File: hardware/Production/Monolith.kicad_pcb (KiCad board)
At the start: 6 copper layers, 43.2 x 74.4 mm, 289 parts, among them J102 Cell 1 NTC wires, J105 Cell 2 NTC wires, J106 Cell 3 NTC wires, J107 Cell 4 NTC wires, J108 PACK- power slot, J109 CELL1 slot, J110 CELL2 slot, J111 CELL3 slot, J112 PACK+ power slot, J113 LOAD PACK_P, J114 LOAD GND, J115 1N Kelvin slot, J116 4P Kelvin slot, J301 TC2030-NL, J302 TC2030-NL GAUGE, J401 TYPE-C 16PCB1.6 IP68, J501 TYPE-C 16PCB1.6 IP68, Q101 AGM404AP1, Q102 AGM404AP1, Q103 AO3400A, Q104 AO3400A, Q401 SiZ240DT, Q402 SiZ240DT, Q501 SiZ240DT, Q502 SiZ240DT, U101 BQ40Z50RSMR-R2, U102 BQ294700DSGR, U204 TPS62177DQCR, U301 CC2340R5MODA, U401 TPS25751DREFR, U402 M24512-DFMC6TG, U403 BQ25756RRVR, U404 TPS62933DRLR, U405 TPD6S300RUKR, U501 TPS25751DREFR, U502 M24512-DFMC6TG, U503 BQ25756RRVR, U504 TPS62933DRLR, U505 TPD6S300RUKR

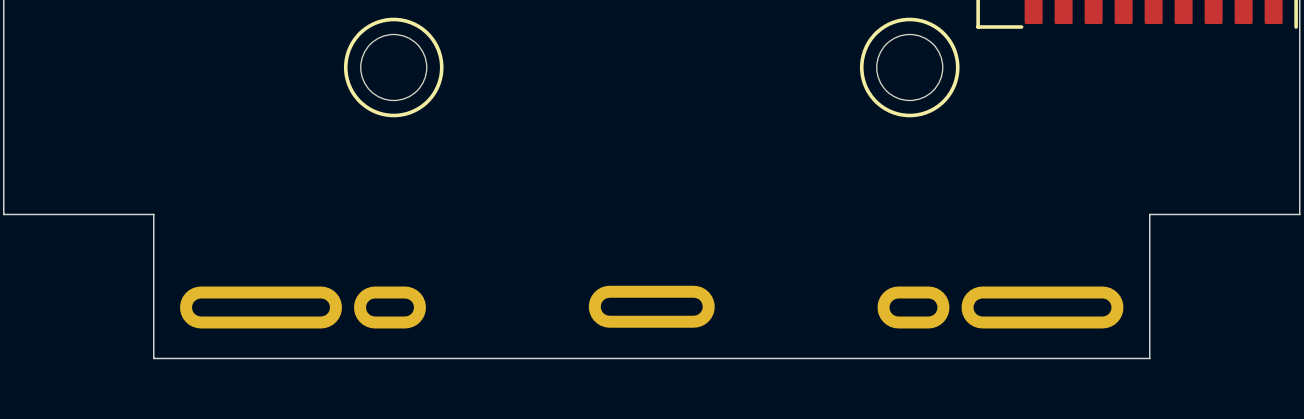
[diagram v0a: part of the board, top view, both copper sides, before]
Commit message: Production board: PACK wire holes for the option C wire tails
J108 / J112 go from the 4.6 mm PACK power slots to Ø1.5 mm plated holes
(0.4 mm ring) for the 18 AWG thin-wall PTFE power wires, at sb_pack_holes():
KiCad (86.975, 135.7255) and (113.025, 135.7255), F.Cu, locked. The Kelvin
wires stay in the J115 / J116 slots.

- make_production.py: WIRE_FP footprint generated from SB_PWIRE_*, used for
  J108 / J112; SLOT_REFS keeps the five slots, WIRE_REFS the two holes.
- make_board.py: --mech also places the wire holes; keepout_list() follows
  the merged model (three tail runs, four KO_B_wire_* from sb_wire_runs()).
- Board: J108 / J112 swapped and placed as Update PCB + --mech would; the four
  PACK / Kelvin finger tail keep-outs replaced by KO_B_wire_*. Other
  keep-outs untouched (KO_F_above_antenna stays removed).
- Schematic Footprint / Value fields and sheet notes; Slot_Tab_4.6x0.6mm
  dropped from the library; README, spec and assembly docs.

KiCad is not available in this environment, so DRC has not been run; a
script check covers the outline, edge rule, ring and courtyards.

Co-Authored-By: Claude Opus 5.5 (1M context) <noreply@anthropic.com>
Claude-Session: https://claude.ai/code/session_01VT5ZsG8mLjRjzAJFn7LJRo
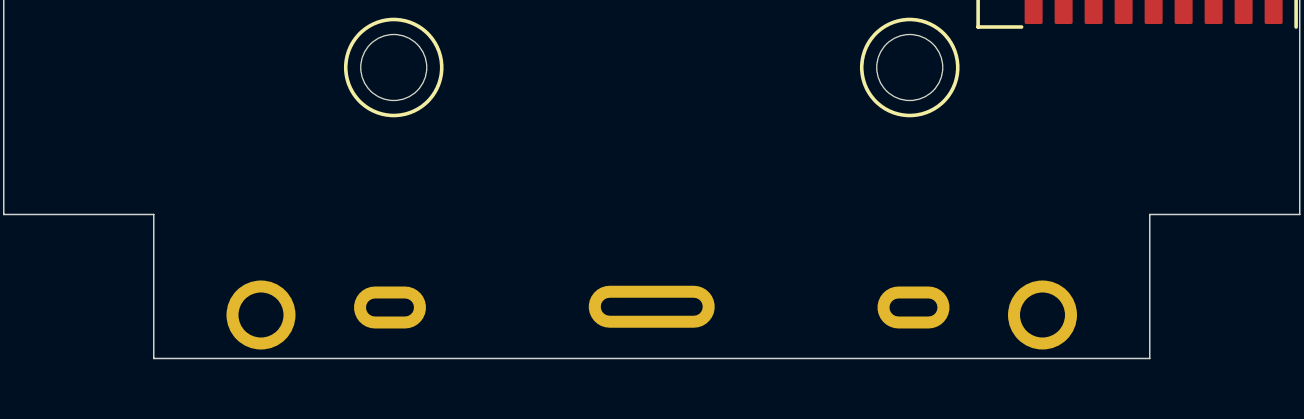
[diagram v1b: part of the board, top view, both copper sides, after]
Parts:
- J108: value PACK- power slot -> PACK- power wire; footprint MonolithDev:Slot_Tab_4.6x0.6mm -> MonolithDev:SolderWire-18AWG_PTFE_1x01_D1.5mm_OD2.3mm
- J112: value PACK+ power slot -> PACK+ power wire; footprint MonolithDev:Slot_Tab_4.6x0.6mm -> MonolithDev:SolderWire-18AWG_PTFE_1x01_D1.5mm_OD2.3mm
- moved J108 0.25 mm to (87.0, 135.7)
- moved J112 0.25 mm to (113.0, 135.7)
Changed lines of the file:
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@@
 		)
 	)
-	(footprint "MonolithDev:Slot_Tab_4.6x0.6mm"
+	(footprint "MonolithDev:SolderWire-18AWG_PTFE_1x01_D1.5mm_OD2.3mm"
 		(locked yes)
 		(layer "F.Cu")
-		(at 113.025 135.4755)
-		(descr "Plated slot 4.6 x 0.6 mm, 0.4 mm ring, for a nickel tail soldered on F.Cu (mechanical/monolith_shell.py sb_slots)")
-		(tags "slot nickel tab battery")
+		(at 113.025 135.7255)
+		(descr "Plated hole 1.5 mm, 0.4 mm ring, for an 18 AWG thin-wall PTFE PACK wire (M22759/11-18, 1.45 mm OD at most) soldered on F.Cu (mechanical/monolith_shell.py sb_pack_holes)")
+		(tags "connector wire 18AWG PTFE battery")
 		(property "Reference" "J112"
-			(at 0 -1.4 0)
+			(at 0 -2 0)
 			(layer "F.SilkS")
 			(hide yes)
@@
 			)
 		)
-		(property "Value" "PACK+ power slot"
-			(at 0 1.4 0)
+		(property "Value" "PACK+ power wire"
+			(at 0 2 0)
 			(layer "F.Fab")
 			(effects
@@
 		(duplicate_pad_numbers_are_jumpers no)
 		(fp_rect
-			(start -2.8 -0.8)
-			(end 2.8 0.8)
+			(start -1.4 -1.4)
+			(end 1.4 1.4)
 			(stroke
 				(width 0.05)
@@
 			(layer "F.CrtYd")
 		)
-		(fp_rect
-			(start -2.3 -0.3)
-			(end 2.3 0.3)
+		(fp_circle
+			(center 0 0)
+			(end 0.725 0)
 			(stroke
 				(width 0.1)
@@
 			)
 		)
-		(pad "1" thru_hole oval
+		(pad "1" thru_hole circle
 			(at 0 0)
-			(size 5.4 1.4)
-			(drill oval 4.6 0.6)
+			(size 2.3 2.3)
+			(drill 1.5)
 			(layers "*.Cu" "*.Mask")
 			(remove_unused_layers no)
@@
 		)
 	)
-	(footprint "MonolithDev:Slot_Tab_4.6x0.6mm"
+	(footprint "MonolithDev:SolderWire-18AWG_PTFE_1x01_D1.5mm_OD2.3mm"
 		(locked yes)
 		(layer "F.Cu")
-		(at 86.975 135.4755)
-		(descr "Plated slot 4.6 x 0.6 mm, 0.4 mm ring, for a nickel tail soldered on F.Cu (mechanical/monolith_shell.py sb_slots)")
-		(tags "slot nickel tab battery")
+		(at 86.975 135.7255)
+		(descr "Plated hole 1.5 mm, 0.4 mm ring, for an 18 AWG thin-wall PTFE PACK wire (M22759/11-18, 1.45 mm OD at most) soldered on F.Cu (mechanical/monolith_shell.py sb_pack_holes)")
+		(tags "connector wire 18AWG PTFE battery")
 		(property "Reference" "J108"
-			(at 0 -1.4 0)
+			(at 0 -2 0)
 			(layer "F.SilkS")
 			(hide yes)
@@
 			)
 		)
-		(property "Value" "PACK- power slot"
-			(at 0 1.4 0)
+		(property "Value" "PACK- power wire"
+			(at 0 2 0)
 			(layer "F.Fab")
 			(effects
@@
 		(duplicate_pad_numbers_are_jumpers no)
 		(fp_rect
-			(start -2.8 -0.8)
-			(end 2.8 0.8)
+			(start -1.4 -1.4)
+			(end 1.4 1.4)
 			(stroke
 				(width 0.05)
@@
 			(layer "F.CrtYd")
 		)
-		(fp_rect
-			(start -2.3 -0.3)
-			(end 2.3 0.3)
+		(fp_circle
+			(center 0 0)
+			(end 0.725 0)
 			(stroke
 				(width 0.1)
@@
 			)
 		)
-		(pad "1" thru_hole oval
+		(pad "1" thru_hole circle
 			(at 0 0)
-			(size 5.4 1.4)
-			(drill oval 4.6 0.6)
+			(size 2.3 2.3)
+			(drill 1.5)
 			(layers "*.Cu" "*.Mask")
 			(remove_unused_layers no)
@@
 	(zone
 		(layer "B.Cu")
-		(name "KO_B_tail_PACKN")
+		(name "KO_B_tail_CELL1")
 		(hatch edge 0.5)
 		(connect_pads yes
@@
 		(polygon
 			(pts
-				(xy 84.375 134.875) (xy 89.575 134.875) (xy 89.575 137.076) (xy 84.375 137.076)
+				(xy 84.1 62.8245) (xy 88.1 62.8245) (xy 88.1 69.9755) (xy 84.1 69.9755)
 			)
 		)
@@
 	(zone
 		(layer "B.Cu")
-		(name "KO_B_tail_1N")
+		(name "KO_B_gap_filler_R")
 		(hatch edge 0.5)
 		(connect_pads yes
@@
 		(polygon
 			(pts
-				(xy 90.175 134.875) (xy 92.375 134.875) (xy 92.375 137.076) (xy 90.175 137.076)
+				(xy 107 88.4755) (xy 116 88.4755) (xy 116 114.475) (xy 107 114.475)
 			)
 		)
@@
 	(zone
 		(layer "B.Cu")
-		(name "KO_B_tail_CELL1")
+		(name "KO_B_rail_R_bottom")
 		(hatch edge 0.5)
 		(connect_pads yes
@@
 		(polygon
 			(pts
-				(xy 84.1 62.8245) (xy 88.1 62.8245) (xy 88.1 69.9755) (xy 84.1 69.9755)
+				(xy 106.5 116.475) (xy 111.3 116.475) (xy 111.3 137.175) (xy 106.5 137.175)
 			)
 		)
@@
 	(zone
 		(layer "B.Cu")
-		(name "KO_B_gap_filler_R")
+		(name "KO_B_tail_CELL2")
 		(hatch edge 0.5)
 		(connect_pads yes
@@
 		(polygon
 			(pts
-				(xy 107 88.4755) (xy 116 88.4755) (xy 116 114.475) (xy 107 114.475)
+				(xy 98 134.875) (xy 102 134.875) (xy 102 137.076) (xy 98 137.076)
 			)
 		)
@@
 	(zone
 		(layer "B.Cu")
-		(name "KO_B_rail_R_bottom")
+		(name "KO_B_rail_R_top")
 		(hatch edge 0.5)
 		(connect_pads yes
@@
 		(polygon
 			(pts
-				(xy 106.5 116.475) (xy 111.3 116.475) (xy 111.3 137.175) (xy 106.5 137.175)
+				(xy 106.5 62.8245) (xy 111.3 62.8245) (xy 111.3 86.4755) (xy 106.5 86.4755)
 			)
 		)
@@
 	(zone
 		(layer "B.Cu")
-		(name "KO_B_tail_CELL2")
+		(name "KO_B_gap_filler_L")
 		(hatch edge 0.5)
 		(connect_pads yes
@@
 		(polygon
 			(pts
-				(xy 98 134.875) (xy 102 134.875) (xy 102 137.076) (xy 98 137.076)
+				(xy 84 88.4755) (xy 93 88.4755) (xy 93 114.475) (xy 84 114.475)
 			)
 		)
@@
 	(zone
 		(layer "B.Cu")
-		(name "KO_B_rail_R_top")
+		(name "KO_B_rail_L_bottom")
 		(hatch edge 0.5)
 		(connect_pads yes
@@
 		(polygon
 			(pts
-				(xy 106.5 62.8245) (xy 111.3 62.8245) (xy 111.3 86.4755) (xy 106.5 86.4755)
+				(xy 88.7 116.475) (xy 93.5 116.475) (xy 93.5 137.175) (xy 88.7 137.175)
 			)
 		)
@@
 	(zone
 		(layer "B.Cu")
-		(name "KO_B_tail_4P")
+		(name "KO_B_tail_CELL3")
 		(hatch edge 0.5)
 		(connect_pads yes
@@
 		(polygon
 			(pts
-				(xy 107.625 134.875) (xy 109.825 134.875) (xy 109.825 137.076) (xy 107.625 137.076)
+				(xy 111.9 62.8245) (xy 115.9 62.8245) (xy 115.9 69.9755) (xy 111.9 69.9755)
 			)
 		)
 	)
+	(embedded_fonts no)
 	(zone
-		(layer "B.Cu")
-		(name "KO_B_gap_filler_L")
+		(layers "B.Cu")
+		(name "KO_B_wire_PACKN")
 		(hatch edge 0.5)
 		(connect_pads yes
@@
 		(polygon
 			(pts
-				(xy 84 88.4755) (xy 93 88.4755) (xy 93 114.475) (xy 84 114.475)
+				(xy 85.75 134.5) (xy 88.2 134.5) (xy 88.2 137.175) (xy 85.75 137.175)
 			)
 		)
 	)
 	(zone
-		(layer "B.Cu")
-		(name "KO_B_tail_PACKP")
+		(layers "B.Cu")
+		(name "KO_B_wire_PACKP")
 		(hatch edge 0.5)
 		(connect_pads yes
@@
 		(polygon
 			(pts
-				(xy 110.425 134.875) (xy 115.625 134.875) (xy 115.625 137.076) (xy 110.425 137.076)
+				(xy 111.8 134.5) (xy 114.25 134.5) (xy 114.25 137.175) (xy 111.8 137.175)
 			)
 		)
 	)
 	(zone
-		(layer "B.Cu")
-		(name "KO_B_rail_L_bottom")
+		(layers "B.Cu")
+		(name "KO_B_wire_1N")
 		(hatch edge 0.5)
 		(connect_pads yes
@@
 		(polygon
 			(pts
-				(xy 88.7 116.475) (xy 93.5 116.475) (xy 93.5 137.175) (xy 88.7 137.175)
+				(xy 90.475 134.675) (xy 92.075 134.675) (xy 92.075 137.175) (xy 90.475 137.175)
 			)
 		)
 	)
 	(zone
-		(layer "B.Cu")
-		(name "KO_B_tail_CELL3")
+		(layers "B.Cu")
+		(name "KO_B_wire_4P")
 		(hatch edge 0.5)
 		(connect_pads yes
@@
 		(polygon
 			(pts
-				(xy 111.9 62.8245) (xy 115.9 62.8245) (xy 115.9 69.9755) (xy 111.9 69.9755)
+				(xy 107.925 134.675) (xy 109.525 134.675) (xy 109.525 137.175) (xy 107.925 137.175)
 			)
 		)
 	)
-	(embedded_fonts no)
 )

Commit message: Production board: front-cell NTC pads, NTC keep-outs, move C421
- J102 / J107 (C1 / C4 NTC lead pads) placed and locked at sb_ntc_pads():
  KiCad (85.3, 77.4755) and (114.7, 77.4755), 90 deg, so pad 2 sits 4 mm up
  the board (z 64 / 68). |y| 14.7 instead of the note's 13.4: at 13.4 J107's
  pad overlapped C406's GND pad.
- KO_B_ntc_C1 / KO_B_ntc_C4 B.Cu keep-outs from sb_ntc_runs() (bead, foam
  cap and lead run up to the pads, 0.5 mm margin).
- C421 moved off the C4 lead run into the B.Cu centre strip at
  (101.6, 88.0), behind port 1's AC_SNS_N bank (C424 / C427).
- monolith_shell.py: SB_NTC_* and sb_ntc_pads() / sb_ntc_runs();
  make_board.py --mech places J102 / J107 and --keepouts draws KO_B_ntc_*.
- Spec, assembly, board README and the NTC note updated.

KiCad is not available here, so DRC has not been run; a script check covers
courtyards, pad clearance, holes, outline and keep-outs. PR #19's PACK holes
and KO_B_wire_* keep-outs are unchanged.

Co-Authored-By: Claude Opus 5.5 (1M context) <noreply@anthropic.com>
Claude-Session: https://claude.ai/code/session_016jEZ67Zn8tgnqsUXippQg9
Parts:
- moved J102 118.7 mm to (85.3, 77.5), turned to 90 degrees
- moved J107 87.3 mm to (114.7, 77.5), turned to 90 degrees
- moved C421 13.6 mm to (101.6, 88.0)
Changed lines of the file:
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@@
 	)
 	(footprint "Connector_Wire:SolderWire-0.15sqmm_1x02_P4mm_D0.5mm_OD1.5mm"
+		(locked yes)
 		(layer "F.Cu")
-		(at 196.247 46.422)
+		(at 114.7 77.4755 90)
 		(descr "Soldered wire connection, for 2 times 0.15 mm² wires, basic insulation, conductor diameter 0.5mm, outer diameter 1.5mm, size source Multi-Contact FLEXI-E 0.15 (https://www.staubli.com/content/dam/ecs/catalogs-brochures/TM/CAB-Main-11014119-en.pdf#page=9), bend radius 3 times outer diameter")
 		(tags "connector wire 0.15sqmm")
 		(property "Reference" "J107"
-			(at 2 -2.05 0)
+			(at 2 -2.05 90)
 			(layer "F.SilkS")
 			(effects
@@
 		)
 		(property "Value" "Cell 4 NTC wires"
-			(at 2 2.05 0)
+			(at 2 2.05 90)
 			(layer "F.Fab")
 			(effects
@@
 		)
 		(property "Datasheet" ""
-			(at 0 0 0)
+			(at 0 0 90)
 			(layer "F.Fab")
 			(hide yes)
@@
 		)
 		(property "Description" ""
-			(at 0 0 0)
+			(at 0 0 90)
 			(layer "F.Fab")
 			(hide yes)
@@
 		)
 		(property "Sourcing" "Hand-solder, not JLC assembled (through-hole; LCSC C492401 PZ254V-11-02P)"
-			(at 0 0 0)
+			(at 0 0 90)
 			(unlocked yes)
 			(layer "F.Fab")
@@
 		)
 		(property "MPN" "PZ254V-11-02P"
-			(at 0 0 0)
+			(at 0 0 90)
 			(unlocked yes)
 			(layer "F.Fab")
@@
 		)
 		(property "Notes" "Wired 10k B3435 NTC (Semitec 103AT-2 class, epoxy bead with insulated leads) taped to the side of BT104, over its sleeve. The can is that cell's negative terminal (about 12.6 V above VSS) and the TS pins are rated 2.1 V: keep the sensor insulated. Gauge internal 18k pull-up; enable TS4 in data flash"
-			(at 0 0 0)
+			(at 0 0 90)
 			(unlocked yes)
 			(layer "F.Fab")
@@
 		)
 		(fp_text user "${REFERENCE}"
-			(at 2 0 90)
+			(at 2 0 180)
 			(layer "F.Fab")
 			(effects
@@
 		)
 		(pad "1" thru_hole roundrect
-			(at 0 0)
+			(at 0 0 90)
 			(size 1.7 1.7)
 			(drill 0.7)
@@
 		)
 		(pad "2" thru_hole circle
-			(at 4 0)
+			(at 4 0 90)
 			(size 1.7 1.7)
 			(drill 0.7)
@@
 	)
 	(footprint "Connector_Wire:SolderWire-0.15sqmm_1x02_P4mm_D0.5mm_OD1.5mm"
+		(locked yes)
 		(layer "F.Cu")
-		(at 196.247 35.172)
+		(at 85.3 77.4755 90)
 		(descr "Soldered wire connection, for 2 times 0.15 mm² wires, basic insulation, conductor diameter 0.5mm, outer diameter 1.5mm, size source Multi-Contact FLEXI-E 0.15 (https://www.staubli.com/content/dam/ecs/catalogs-brochures/TM/CAB-Main-11014119-en.pdf#page=9), bend radius 3 times outer diameter")
 		(tags "connector wire 0.15sqmm")
 		(property "Reference" "J102"
-			(at 2 -2.05 0)
+			(at 2 -2.05 90)
 			(layer "F.SilkS")
 			(effects
@@
 		)
 		(property "Value" "Cell 1 NTC wires"
-			(at 2 2.05 0)
+			(at 2 2.05 90)
 			(layer "F.Fab")
 			(effects
@@
 		)
 		(property "Datasheet" ""
-			(at 0 0 0)
+			(at 0 0 90)
 			(layer "F.Fab")
 			(hide yes)
@@
 		)
 		(property "Description" "Generic connector, single row, 01x02, script generated (kicad-library-utils/schlib/autogen/connector/)"
-			(at 0 0 0)
+			(at 0 0 90)
 			(layer "F.Fab")
 			(hide yes)
@@
 		)
 		(property "Sourcing" "Hand-solder, not JLC assembled (through-hole; LCSC C492401 PZ254V-11-02P)"
-			(at 0 0 0)
+			(at 0 0 90)
 			(unlocked yes)
 			(layer "F.Fab")
@@
 		)
 		(property "MPN" "PZ254V-11-02P"
-			(at 0 0 0)
+			(at 0 0 90)
 			(unlocked yes)
 			(layer "F.Fab")
@@
 		)
 		(property "Notes" "Wired 10k B3435 NTC (Semitec 103AT-2 class, epoxy bead with insulated leads) taped to the side of BT101, over its sleeve. The can is that cell's negative terminal (at VSS) and the TS pins are rated 2.1 V: keep the sensor insulated. Gauge internal 18k pull-up; enable TS1 in data flash"
-			(at 0 0 0)
+			(at 0 0 90)
 			(unlocked yes)
 			(layer "F.Fab")
@@
 		)
 		(fp_text user "${REFERENCE}"
-			(at 2 0 90)
+			(at 2 0 180)
 			(layer "F.Fab")
 			(effects
@@
 		)
 		(pad "1" thru_hole roundrect
-			(at 0 0)
+			(at 0 0 90)
 			(size 1.7 1.7)
 			(drill 0.7)
@@
 		)
 		(pad "2" thru_hole circle
-			(at 4 0)
+			(at 4 0 90)
 			(size 1.7 1.7)
 			(drill 0.7)
@@
 	(footprint "Capacitor_Tantalum_SMD:CP_EIA-7343-31_Kemet-D"
 		(layer "B.Cu")
-		(at 113.8174 82.0166 90)
+		(at 101.6 88 90)
 		(descr "Tantalum Capacitor SMD Kemet-D (7343-31 Metric), IPC-7352 nominal, (Body size from: http://www.kemet.com/Lists/ProductCatalog/Attachments/253/KEM_TC101_STD.pdf)")
 		(tags "capacitor tantalum")
@@
 			)
 		)
+	)
+	(zone
+		(layers "B.Cu")
+		(name "KO_B_ntc_C1")
+		(hatch edge 0.5)
+		(connect_pads yes
+			(clearance 0)
+		)
+		(min_thickness 0.25)
+		(keepout
+			(tracks allowed)
+			(vias allowed)
+			(pads allowed)
+			(copperpour allowed)
+			(footprints not_allowed)
+		)
+		(placement
+			(enabled no)
+			(sheetname "")
+		)
+		(fill
+			(thermal_gap 0.5)
+			(thermal_bridge_width 0.5)
+			(island_removal_mode 0)
+		)
+		(polygon
+			(pts
+				(xy 83.95 72.1255) (xy 88.5 72.1255) (xy 88.5 96.4755) (xy 83.95 96.4755)
+			)
+		)
+	)
+	(zone
+		(layers "B.Cu")
+		(name "KO_B_ntc_C4")
+		(hatch edge 0.5)
+		(connect_pads yes
+			(clearance 0)
+		)
+		(min_thickness 0.25)
+		(keepout
+			(tracks allowed)
+			(vias allowed)
+			(pads allowed)
+			(copperpour allowed)
+			(footprints not_allowed)
+		)
+		(placement
+			(enabled no)
+			(sheetname "")
+		)
+		(fill
+			(thermal_gap 0.5)
+			(thermal_bridge_width 0.5)
+			(island_removal_mode 0)
+		)
+		(polygon
+			(pts
+				(xy 111.5 72.1255) (xy 116.05 72.1255) (xy 116.05 96.4755) (xy 111.5 96.4755)
+			)
+		)
